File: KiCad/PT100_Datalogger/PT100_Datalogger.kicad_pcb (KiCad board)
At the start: 4 copper layers, 90 x 122 mm, 190 parts, among them J1 PWR, J10 Conn_01x03, J11 Conn_01x03, J12 Conn_01x03, J13 HLK-LD2410C, J14 691406710003B, J2 USB_C_Receptacle, J3 Screw_Terminal_01x02, J4 CT, J5 SJ1-3523N, J6 JTAG, J7 CT_SW, J8 Conn_01x03, J9 Conn_01x03, K1 J115F11CH5VDCS61.5U, Q10 BSS806NEH6327XTSA1, Q11 SSM3J36FS,LF, Q12 SSM3J36FS,LF, Q13 SSM3J36FS,LF, Q14 BSS806NEH6327XTSA1, Q15 SSM3J36FS,LF, Q16 MMBT3904, Q17 MMBT3904, Q3 BSS806NEH6327XTSA1, Q4 BSS806NEH6327XTSA1, Q5 BSS806NEH6327XTSA1, Q6 BSS806NEH6327XTSA1, Q7 BSS806NEH6327XTSA1, Q8 BSS806NEH6327XTSA1, Q9 BSS806NEH6327XTSA1, SW3 SW_Push_Shielded, SW4 SW_Push_Shielded, SW5 SW_Push_Shielded, SW6 SW_Push_Shielded, SW7 SW_Push_Shielded, U1 ESP32-S3-WROOM-1-N8R2, U10 SHT4x, U11 PCF85263AT, U12 FM24CL16B-GTR, U13 MCP9601, U2 CP2102N-Axx-xQFN28, U3 NCS2250SQ2T2G, U4 LDL212PV33R, U5 TMP1075DSG, U6 INND-TS56RAB, U7 INND-TS56RAB, U8 INND-TS56RAB, U9 INND-TS56RAB, Y1 32.768K12.5PI/3215E

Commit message: Finished KiCad PCB REV A
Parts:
- removed D10, D6: ESD5Z12T1G, Diode_SMD:D_SOD-523
- removed D26, D30, D31, D32, D33, D36: ESD5Z3V3, Diode_SMD:D_SOD-523
- removed D27, D37, D38: B5819W, Diode_SMD:D_SOD-123
- removed K1: J115F11CH5VDCS61.5U, Personal:J115FX
- removed MK2: ICS-43434, Sensor_Audio:InvenSense_ICS-43434-6_3.5x2.65mm
- removed Q10, Q14, Q3, Q4, Q5, Q6, Q7, Q8, Q9: BSS806NEH6327XTSA1, Package_TO_SOT_SMD:SOT-23-3
- removed Q11, Q12, Q13, Q15: SSM3J36FS,LF, Package_TO_SOT_SMD:SOT-416
- removed Q16, Q17: MMBT3904, Package_TO_SOT_SMD:SOT-23_Handsoldering
- removed R30, R32, R34, R36, R38, R40, R47, R51: 1K, Resistor_SMD:R_0603_1608Metric_Pad0.98x0.95mm_HandSolder
- removed R31, R33, R35, R37, R39, R46, R50, R57: 100K, Resistor_SMD:R_0603_1608Metric_Pad0.98x0.95mm_HandSolder
- removed R43: 1M, Resistor_SMD:R_0603_1608Metric_Pad0.98x0.95mm_HandSolder
- removed R44, R45: 10k, Resistor_SMD:R_0603_1608Metric_Pad0.98x0.95mm_HandSolder
- removed R48: 4K7, Resistor_SMD:R_0603_1608Metric_Pad0.98x0.95mm_HandSolder
- removed R49: 220R, Resistor_SMD:R_0603_1608Metric_Pad0.98x0.95mm_HandSolder
- removed R58, R59, R60: 51R, Resistor_SMD:R_0603_1608Metric_Pad0.98x0.95mm_HandSolder
- removed R62, R63, R64, R65, R66, R67, R68, R69: 22R, Resistor_SMD:R_0603_1608Metric_Pad0.98x0.95mm_HandSolder
- removed RV1: PV36Y102C01B00, Personal:TRIM_PV36Y102C01B00
- removed U11: PCF85263AT, Package_SO:SOIC-8_3.9x4.9mm_P1.27mm
- removed U12: FM24CL16B-GTR, Package_SO:SOIC-8_3.9x4.9mm_P1.27mm
- removed Y1: 32.768K12.5PI/3215E, Crystal:Crystal_SMD_3215-2Pin_3.2x1.5mm
- added C25: 100nF, Capacitor_SMD:C_0603_1608Metric_Pad1.08x0.95mm_HandSolder, F.Cu at (94.4, 141.1)
- added C26: 100nF, Capacitor_SMD:C_0603_1608Metric_Pad1.08x0.95mm_HandSolder, F.Cu at (105.0, 141.1)
- added C27: 100nF, Capacitor_SMD:C_0603_1608Metric_Pad1.08x0.95mm_HandSolder, F.Cu at (109.7, 129.3)
- added C28: 100nF, Capacitor_SMD:C_0603_1608Metric_Pad1.08x0.95mm_HandSolder, F.Cu at (101.3, 77.0)
- added C29: 10uF, Capacitor_SMD:C_0805_2012Metric_Pad1.18x1.45mm_HandSolder, F.Cu at (99.3, 77.5)
- added D14: TSD05CDYFR, Diode_SMD:D_SOD-323_HandSoldering, F.Cu at (63.8, 70.8)
- added D15: ESD5Z3V3, Diode_SMD:D_SOD-523, F.Cu at (91.6, 130.4)
- added JP3: SolderJumper_3_Bridged12, Jumper:SolderJumper-3_P1.3mm_Bridged12_RoundedPad1.0x1.5mm, F.Cu at (99.0, 130.7)
- added JP5: SolderJumper_3_Bridged12, Jumper:SolderJumper-3_P1.3mm_Bridged12_RoundedPad1.0x1.5mm, F.Cu at (88.4, 141.5)
- added JP6: SolderJumper_3_Bridged12, Jumper:SolderJumper-3_P1.3mm_Bridged12_RoundedPad1.0x1.5mm, F.Cu at (99.0, 141.5)
- added JP7: SolderJumper_3_Bridged12, Jumper:SolderJumper-3_P1.3mm_Bridged12_Pad1.0x1.5mm, F.Cu at (95.1, 91.6)
- added JP8: SolderJumper_2_Open, Jumper:SolderJumper-2_P1.3mm_Open_TrianglePad1.0x1.5mm, F.Cu at (99.9, 91.5)
- added JP9: SolderJumper_2_Open, Jumper:SolderJumper-2_P1.3mm_Open_TrianglePad1.0x1.5mm, F.Cu at (96.0, 96.3)
- C12, C7: value 10uF -> 100nF; footprint Capacitor_SMD:C_0805_2012Metric_Pad1.18x1.45mm_HandSolder -> Capacitor_SMD:C_0603_1608Metric_Pad1.08x0.95mm_HandSolder
- C14: value 100nF -> 22uF; footprint Capacitor_SMD:C_0603_1608Metric_Pad1.08x0.95mm_HandSolder -> Capacitor_SMD:C_0805_2012Metric_Pad1.18x1.45mm_HandSolder
- C15: value 10uF -> 22uF
- C6: value 10uF -> DE1B3RA471KN4AP01F; footprint Capacitor_SMD:C_0805_2012Metric_Pad1.18x1.45mm_HandSolder -> Capacitor_THT:C_Disc_D7.5mm_W5.0mm_P10.00mm
- D11, D8: value TSD05CDYFR -> ESD5Z12T1G; footprint Diode_SMD:D_SOD-323_HandSoldering -> Diode_SMD:D_SOD-523
- D12: value TSD05CDYFR -> ESD5Z3V3; footprint Diode_SMD:D_SOD-323_HandSoldering -> Diode_SMD:D_SOD-523
- D2: value LED -> TSD05CDYFR; footprint LED_THT:LED_D5.0mm -> Diode_SMD:D_SOD-323_HandSoldering
- D21, D4: footprint LED_THT:LED_D5.0mm -> LED_SMD:LED_0603_1608Metric_Pad1.05x0.95mm_HandSolder
- D3: value SM4007PL -> TSD05CDYFR; footprint Diode_SMD:D_SOD-123F -> Diode_SMD:D_SOD-323_HandSoldering
- D5: value SM4007PL -> B5819W; footprint Diode_SMD:D_SOD-123F -> Diode_SMD:D_SOD-123
- D9: value B5819W -> ESD5Z12T1G; footprint Diode_SMD:D_SOD-123 -> Diode_SMD:D_SOD-523
- H1: footprint MountingHole:MountingHole_3.2mm_M3 -> MountingHole:MountingHole_3.2mm_M3_Pad
- J10: value Conn_01x03 -> DIG3
- J11: value Conn_01x03 -> DIG4
- J12: value Conn_01x03 -> DIG5
- J13: value HLK-LD2410C -> DIG6; footprint Connector_Molex:Molex_KK-254_AE-6410-05A_1x05_P2.54mm_Vertical -> Connector_Molex:Molex_KK-254_AE-6410-03A_1x03_P2.54mm_Vertical
- J14: value 691406710003B -> PWR; footprint Personal:691406710003B -> Connector_JST:JST_VH_B3P-VH_1x03_P3.96mm_Vertical
- J2: value USB_C_Receptacle -> Conn_01x04; footprint Personal:CONN_CU3216SASBLR004-NH_CVI -> Connector_Molex:Molex_KK-254_AE-6410-04A_1x04_P2.54mm_Vertical
- J3: value Screw_Terminal_01x02 -> TC
- J4: value CT -> MSD-4-A; footprint Connector_Molex:Molex_KK-254_AE-6410-02A_1x02_P2.54mm_Vertical -> Personal:CUI_MSD-4-A
- J5: value SJ1-3523N -> CU3216SASBLR004-NH; footprint Connector_Audio:Jack_3.5mm_CUI_SJ1-3523N_Horizontal -> Personal:CONN_CU3216SASBLR004-NH_CVI
- J6: value JTAG -> RTD; footprint Connector_PinHeader_1.27mm:PinHeader_2x05_P1.27mm_Vertical -> Connector_Molex:Molex_KK-254_AE-6410-05A_1x05_P2.54mm_Vertical
- J7: value CT_SW -> MAX7219; footprint Connector_Molex:Molex_KK-254_AE-6410-02A_1x02_P2.54mm_Vertical -> Connector_Molex:Molex_KK-254_AE-6410-05A_1x05_P2.54mm_Vertical
- J8: value Conn_01x03 -> DIG1
- J9: value Conn_01x03 -> DIG2
- JP1: value SolderJumper_3_Open -> SolderJumper_3_Bridged12; footprint Jumper:SolderJumper-3_P1.3mm_Open_Pad1.0x1.5mm -> Jumper:SolderJumper-3_P1.3mm_Bridged12_RoundedPad1.0x1.5mm
- JP2: value SolderJumper_2_Open -> SolderJumper_3_Bridged12; footprint Jumper:SolderJumper-2_P1.3mm_Open_Pad1.0x1.5mm -> Jumper:SolderJumper-3_P1.3mm_Bridged12_RoundedPad1.0x1.5mm
- JP4: value SolderJumper_2_Bridged -> SolderJumper_3_Bridged12; footprint Jumper:SolderJumper-2_P1.3mm_Bridged_Pad1.0x1.5mm -> Jumper:SolderJumper-3_P1.3mm_Bridged12_RoundedPad1.0x1.5mm
- R15, R26, R28: value 1K -> 100R
- R16, R25, R27, R29: value 100K -> 100R
- R17: value 5k1 -> 10K
- R18: value 5k1 -> 100R
- R2: value 1K -> 10K
- R21: value 100K -> RN73H1JTTD3920A05
- R22: value 1K -> 330R
- R23: value 100K -> 5k1
- R24: value 1K -> 5k1
- R3: value 22K1 -> 10K
- R4: value 47K5 -> 10K
- R7: value 50R -> 100R
- R8: value 100 -> 100R
- SW3, SW4, SW5, SW6, SW7: footprint Personal:SW_1825955-6_TEC -> Button_Switch_SMD:SW_SPST_B3U-1100P
- U10: value SHT4x -> SHT45
- U2: value CP2102N-Axx-xQFN28 -> SN74LVC245APW; footprint Package_DFN_QFN:QFN-28-1EP_5x5mm_P0.5mm_EP3.35x3.35mm -> Package_SO:TSSOP-20_4.4x6.5mm_P0.65mm
- U3: value NCS2250SQ2T2G -> MAX31865xAP; footprint Package_TO_SOT_SMD:SOT-353_SC-70-5_Handsoldering -> Package_SO:SSOP-20_5.3x7.2mm_P0.65mm
- U5: value TMP1075DSG -> TPD2E001; footprint Package_SON:WSON-8-1EP_2x2mm_P0.5mm_EP0.9x1.6mm_ThermalVias -> Package_TO_SOT_SMD:SOT-553
- U6: value INND-TS56RAB -> TPD2E001; footprint Display_7Segment:7SegmentLED_LTS6760_LTS6780 -> Package_TO_SOT_SMD:SOT-553
- U7: value INND-TS56RAB -> CY15B104QN-50SXI; footprint Display_7Segment:7SegmentLED_LTS6760_LTS6780 -> Package_SO:SOIC-8_5.3x5.3mm_P1.27mm
- U8: value INND-TS56RAB -> PCF2131; footprint Display_7Segment:7SegmentLED_LTS6760_LTS6780 -> Personal:16-HLSON
- U9: value INND-TS56RAB -> TPD6E05U06RVZ; footprint Display_7Segment:7SegmentLED_LTS6760_LTS6780 -> Package_SON:Texas_R-PUSON-N14
- moved J1 183.2 mm to (57.3, 83.8)
- moved J5 177.1 mm to (61.0, 70.1), turned to -90 degrees
- moved D7 172.5 mm to (63.8, 84.0), turned to -90 degrees
- moved C1 171.2 mm to (66.5, 51.0), turned to -90 degrees
- moved C2 171.1 mm to (64.7, 51.2), turned to -90 degrees
- moved C8 167.0 mm to (73.5, 75.0), turned to 90 degrees
- moved H3 164.9 mm to (56.5, 148.0)
- moved C21 164.9 mm to (70.9, 79.9), turned to 0 degrees
- moved C5 164.6 mm to (54.0, 64.7), turned to -90 degrees
- moved C4 162.4 mm to (54.0, 59.8), turned to -90 degrees
- moved D29 162.3 mm to (55.5, 64.7), turned to -90 degrees
- moved C3 160.9 mm to (62.0, 61.4)
- moved D28 160.1 mm to (55.5, 59.8), turned to -90 degrees
- moved D5 160.0 mm to (63.8, 79.3), turned to 90 degrees
- moved R1 155.2 mm to (62.0, 63.0)
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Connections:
- C10 pad 1: TEMP_DOWN -> STOP
- C11 pad 1: SOFT_ON_OFF -> UNITS
- C12 pad 1: Net-(D27-K) -> Net-(JP9-A)
- C12 pad 2: GND -> Net-(JP8-B)
- C13 pad 1: Net-(D16-A2) -> +3V3
- C14 pad 1: +3V3 -> Net-(U8-IFS)
- C15 pad 1: Net-(J4-Pin_1) -> Net-(U8-IFS)
- C15 pad 2: Net-(D27-A) -> GND
- C16 pad 1: CT -> +5V
- C18 pad 1: +3V3 -> DIGITAL_2
- C20 pad 1: +3V3 -> DIGITAL_3
- C21 pad 1: +3V3 -> Net-(U8-IFS)
- C24 pad 1: +3V3 -> DIGITAL_4
- C6 pad 1: +3V3 -> Earth_Clean
- C7 pad 1: Net-(U2-VBUS) -> DIGITAL_1
- C9 pad 1: TEMP_UP -> START
- D1 pad 1: GND -> VSense
- D1 pad 2: VSense -> GND
- D11 pad 1: GND -> Net-(D11-K)
- D11 pad 2: USB_D+ -> GND
- D12 pad 1: GND -> SD_SW
- D12 pad 2: USB_D- -> GND
- D13 pad 1: GND -> Net-(D13-K)
- D13 pad 2: Net-(D13-A2) -> GND
- D16 pad 1: GND -> Net-(D16-K)
- D16 pad 2: Net-(D16-A2) -> GND
- D17 pad 1: GND -> Net-(D17-K)
- D17 pad 2: Net-(D17-A2) -> GND
- D18 pad 1: GND -> Net-(D18-K)
- D18 pad 2: Net-(D18-A2) -> GND
- D19 pad 1: GND -> Net-(D19-K)
- D19 pad 2: Net-(D19-A2) -> GND
- D2 pad 1: Net-(D2-K) -> GND
- D2 pad 2: Net-(D2-A) -> USB_D-
- D22 pad 1: GND -> Net-(D22-K)
- D22 pad 2: ONEWIRE -> GND
- D23 pad 1: GND -> Net-(D23-K)
- D23 pad 2: MTMS -> GND
- D24 pad 1: GND -> Net-(D24-K)
- D24 pad 2: MTCK -> GND
- D25 pad 1: GND -> Net-(D25-K)
- D25 pad 2: MTDO -> GND
- D28 pad 1: GND -> GPIO0
- D28 pad 2: GPIO0 -> GND
- D29 pad 1: GND -> CHIP_PU
- D29 pad 2: CHIP_PU -> GND
- D3 pad 1: +5V -> GND
- D3 pad 2: Net-(D2-K) -> VBUS
- D34 pad 1: GND -> U0RXD
- D34 pad 2: U1TX -> GND
- D35 pad 1: GND -> U0TXD
- D35 pad 2: U1RX -> GND
- D5 pad 1: +3V3 -> +5V
- D5 pad 2: Net-(D27-K) -> VBUS
- D8 pad 1: GND -> Net-(D8-K)
- D8 pad 2: VBUS -> GND
- D9 pad 1: +5V -> Net-(D9-K)
- D9 pad 2: VBUS -> GND
- H3 pad 1: GND -> unconnected-(H3-Pad1)
- J10 pad 1: +3V3 -> Net-(J10-Pin_1)
- J10 pad 2: ONEWIRE -> Net-(D22-K)
- J11 pad 1: +3V3 -> Net-(J11-Pin_1)
- J11 pad 2: ONEWIRE -> Net-(D23-K)
- J12 pad 1: +3V3 -> Net-(J12-Pin_1)
- J12 pad 2: ONEWIRE -> Net-(D24-K)
- J13 pad 1: U1RX -> Net-(J13-Pin_1)
- J13 pad 2: U1TX -> Net-(D25-K)
- J13 pad 3: MM_OUT -> GND
- J14 pad 3: AC_OUT -> Earth_Clean
- J3 pad 1: GND -> Net-(D13-K)
- J3 pad 3: Net-(D13-A2) -> GND
- J4 pad 1: Net-(J4-Pin_1) -> SD_D2
- J4 pad 2: GND -> SD_D3
- J6 pad 1: +3V3 -> GND
- J6 pad 2: MTMS -> RTD_FN
- J6 pad 3: GND -> RTD_INN
- J6 pad 4: MTCK -> RTD_INP
- J6 pad 5: GND -> RTD_FP
- J7 pad 1: CT -> +5V
- J8 pad 1: +3V3 -> Net-(J8-Pin_1)
- J8 pad 2: ONEWIRE -> Net-(D16-K)
- J9 pad 1: +3V3 -> Net-(J9-Pin_1)
- J9 pad 2: ONEWIRE -> Net-(D15-K)
- JP1 pad 1: Net-(JP1-A) -> +3V3
- JP1 pad 2: Net-(D16-A2) -> Net-(J8-Pin_1)
- JP1 pad 3: CT -> +5V
- JP2 pad 1: Net-(JP2-A) -> +3V3
- JP2 pad 2: CT -> Net-(J9-Pin_1)
- JP4 pad 1: Net-(JP4-A) -> +3V3
- JP4 pad 2: CHIP_PU -> Net-(J11-Pin_1)
- R10 pad 1: Net-(D17-A2) -> Net-(D17-K)
- R11 pad 1: Net-(D18-A2) -> Net-(D18-K)
- R12 pad 1: Net-(D18-A2) -> Net-(D18-K)
- R12 pad 2: TEMP_DOWN -> STOP
- R13 pad 1: Net-(D19-A2) -> Net-(D19-K)
- R14 pad 1: Net-(D19-A2) -> Net-(D19-K)
- R14 pad 2: SOFT_ON_OFF -> UNITS
- R15 pad 1: SEG_A -> Net-(JP8-B)
- R15 pad 2: Net-(Q3-G) -> RTD_INN
- R16 pad 1: GND -> Net-(JP8-A)
- R16 pad 2: SEG_A -> RTD_FN
- R17 pad 1: Net-(J2-CC1) -> +3V3
- R17 pad 2: GND -> SD_D1
- R18 pad 1: Net-(J2-CC2) -> Net-(D15-K)
- R18 pad 2: GND -> DIGITAL_2
- R2 pad 2: Net-(U2-~{RST}) -> SD_D2
- R21 pad 1: GND -> Net-(U3-BIAS)
- R21 pad 2: SEG_B -> Net-(U3-ISENSOR)
- R22 pad 1: SEG_B -> +3V3
- R22 pad 2: Net-(Q4-G) -> Net-(U8-IFS)
- R23 pad 1: GND -> Net-(J5-CC1)
- R23 pad 2: SEG_C -> GND
- R24 pad 1: SEG_C -> Net-(J5-CC2)
- R24 pad 2: Net-(Q5-G) -> GND
- R25 pad 1: GND -> Net-(D16-K)
- R25 pad 2: SEG_D -> DIGITAL_1
- R26 pad 1: SEG_D -> Net-(D22-K)
- R26 pad 2: Net-(Q6-G) -> DIGITAL_3
- R27 pad 1: GND -> Net-(D23-K)
- R27 pad 2: SEG_E -> DIGITAL_4
- R28 pad 1: SEG_E -> Net-(D24-K)
- R28 pad 2: Net-(Q7-G) -> DIGITAL_5
- R29 pad 1: GND -> Net-(D25-K)
- R29 pad 2: SEG_F -> DIGITAL_6
- R3 pad 1: VBUS -> +3V3
- R3 pad 2: Net-(U2-VBUS) -> SD_D3
- R4 pad 1: Net-(U2-VBUS) -> +3V3
- R4 pad 2: GND -> SD_CMD
- R5 pad 1: DTR -> +3V3
- R5 pad 2: Net-(Q16-B) -> SD_CLK
- R52 pad 1: Net-(D13-A2) -> Net-(D13-K)
- R56 pad 1: Net-(D13-A2) -> Net-(D13-K)
- R6 pad 1: RTS -> +3V3
- R6 pad 2: Net-(Q17-B) -> SD_D0
- R7 pad 1: Net-(J4-Pin_1) -> Net-(JP7-B)
- R7 pad 2: GND -> RTD_FP
- R8 pad 1: Net-(D27-K) -> Net-(JP9-A)
- R8 pad 2: Net-(D16-A2) -> RTD_INP
- R9 pad 1: Net-(D17-A2) -> Net-(D17-K)
- R9 pad 2: TEMP_UP -> START
- SW3 pad 2: Net-(D17-A2) -> Net-(D17-K)
- SW4 pad 2: Net-(D18-A2) -> Net-(D18-K)
- SW5 pad 2: Net-(D19-A2) -> Net-(D19-K)
- U1 pad 10: U1TX -> DIGITAL_4
- U1 pad 11: U1RX -> LEVEL_OE
- U1 pad 13: SEG_DP -> USB_D-
- U1 pad 14: ALERT -> USB_D+
- U1 pad 18: SEG_A -> MAX_CS
- U1 pad 19: SEG_B -> MOSI
- U1 pad 20: SEG_C -> SCK
- U1 pad 21: SEG_D -> MISO
- U1 pad 22: SEG_E -> DIGITAL_2
- U1 pad 23: DIG_1 -> DIGITAL_5
- U1 pad 24: DIG_2 -> D_CS
- U1 pad 25: DIG_3 -> SD_SW
- U1 pad 28: Net-(U1-IO35) -> SD_D1
- U1 pad 29: I2S_D -> SD_D0
- U1 pad 30: Net-(U1-IO37) -> SD_CLK
- U1 pad 31: RELAY_PWR -> SD_CMD
- U1 pad 32: MTCK -> SD_D3
- U1 pad 33: MTDO -> SD_D2
- U1 pad 34: MTDI -> ~{MAX_RDY}
- U1 pad 35: MTMS -> DIGITAL_6
- U1 pad 38: DIG_4 -> RTC_INT
- U1 pad 39: ONEWIRE -> 1HZ
- U1 pad 4: SOFT_ON_OFF -> DIGITAL_1
- U1 pad 5: TEMP_DOWN -> START
- U1 pad 6: TEMP_UP -> STOP
- U1 pad 7: CT -> UNITS
- U1 pad 8: SEG_F -> FRAM_CS
- U1 pad 9: SEG_G -> DIGITAL_3
- U2 pad 1: unconnected-(U2-~{DCD}-Pad1) -> +5V
- U2 pad 10: unconnected-(U2-NC-Pad10) -> GND
- U2 pad 16: unconnected-(U2-~{WAKEUP}/GPIO.3-Pad16) -> Net-(D8-K)
- U2 pad 17: unconnected-(U2-RS485/GPIO.2-Pad17) -> Net-(D9-K)
- U2 pad 18: unconnected-(U2-~{RXT}/GPIO.1-Pad18) -> Net-(D11-K)
- U2 pad 19: unconnected-(U2-~{TXT}/GPIO.0-Pad19) -> LEVEL_OE
- U2 pad 2: unconnected-(U2-~{RI}/CLK-Pad2) -> MOSI
- U2 pad 20: unconnected-(U2-GPIO.6-Pad20) -> +5V
- U2 pad 3: GND -> D_CS
- U2 pad 4: USB_D+ -> SCK
- U2 pad 5: USB_D- -> GND
- U2 pad 6: +3V3 -> GND
- U2 pad 7: +3V3 -> GND
- U2 pad 8: Net-(U2-VBUS) -> GND
- U2 pad 9: Net-(U2-~{RST}) -> GND
- U3 pad 1: Net-(JP2-A) -> ~{MAX_RDY}
- U3 pad 2: GND -> +3V3
- U3 pad 3: Net-(JP1-A) -> +3V3
- U3 pad 4: Net-(U3--) -> Net-(U3-BIAS)
- U3 pad 5: +3V3 -> Net-(U3-BIAS)
- U5 pad 1: SDA -> +3V3
- U5 pad 2: SCL -> unconnected-(U5-NC-Pad2)
- U5 pad 3: RELAY_ALERT -> RTD_INP
- U5 pad 5: GND -> RTD_FP
- U6 pad 1: SEG_E_LED -> +3V3
- U6 pad 2: SEG_D_LED -> unconnected-(U6-NC-Pad2)
- U6 pad 3: DIG_1_LED -> RTD_FN
- U6 pad 4: SEG_C_LED -> GND
- U6 pad 5: SEG_DP_LED -> RTD_INN
- U7 pad 1: SEG_E_LED -> FRAM_CS
- U7 pad 2: SEG_D_LED -> MISO
- U7 pad 3: DIG_2_LED -> +3V3
- U7 pad 4: SEG_C_LED -> GND
- U7 pad 5: SEG_DP_LED -> MOSI
- U7 pad 6: SEG_B_LED -> SCK
- U7 pad 7: SEG_A_LED -> unconnected-(U7-~{HOLD}-Pad7)
- U7 pad 8: DIG_2_LED -> +3V3
- U8 pad 1: SEG_E_LED -> Net-(U8-IFS)
- U8 pad 10: SEG_G_LED -> unconnected-(U8-~{TS3}-Pad10)
- U8 pad 2: SEG_D_LED -> SCL
- U8 pad 3: DIG_3_LED -> GND
- U8 pad 4: SEG_C_LED -> GND
- U8 pad 5: SEG_DP_LED -> SDA
- U8 pad 6: SEG_B_LED -> 1HZ
- U8 pad 7: SEG_A_LED -> GND
- U8 pad 8: DIG_3_LED -> unconnected-(U8-~{TS1}-Pad8)
- U8 pad 9: SEG_F_LED -> unconnected-(U8-~{TS2}-Pad9)
- U9 pad 1: SEG_E_LED -> SD_D2
- U9 pad 10: SEG_G_LED -> GND
- U9 pad 2: SEG_D_LED -> SD_D3
- U9 pad 3: DIG_4_LED -> SD_CMD
- U9 pad 4: SEG_C_LED -> SD_CLK
- U9 pad 5: SEG_DP_LED -> GND
- U9 pad 6: SEG_B_LED -> SD_D0
- U9 pad 7: SEG_A_LED -> SD_D1
- U9 pad 8: DIG_4_LED -> SD_D1
- U9 pad 9: SEG_F_LED -> SD_D0
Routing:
- net ONEWIRE: track 163.7 -> 0.00 mm, vias 2 -> 0
- net SEG_E_LED: track 116.2 -> 0.00 mm, vias 2 -> 0
- net DIGITAL_4: track 0.00 -> 102.3 mm, vias 0 -> 2
- net DIGITAL_6: track 0.00 -> 99.2 mm, vias 0 -> 2
- net DIGITAL_1: track 0.00 -> 98.3 mm, vias 0 -> 2
- net SEG_C_LED: track 95.7 -> 0.00 mm, vias 1 -> 0
- net SEG_D_LED: track 94.7 -> 0.00 mm, vias 1 -> 0
- net SEG_DP_LED: track 94.6 -> 0.00 mm, vias 1 -> 0
- net DIGITAL_3: track 0.00 -> 93.8 mm, vias 0 -> 2
- net RELAY_ALERT: track 87.0 -> 0.00 mm, vias 2 -> 0
- net START: track 0.00 -> 87.0 mm, vias 0 -> 2
- net UNITS: track 0.00 -> 86.7 mm, vias 0 -> 2
- net STOP: track 0.00 -> 85.0 mm, vias 0 -> 2
- net DIGITAL_5: track 0.00 -> 81.8 mm, vias 0 -> 2
- net SEG_E: track 80.9 -> 0.00 mm, vias 3 -> 0
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- removed copper zone on B.Cu, net AC_OUT
- removed copper zone on F.Cu, net AC_OUT
- removed copper zone on In1.Cu, net AC_OUT
- removed copper zone on In2.Cu, net AC_OUT
- removed copper zone on F.Cu, net GND
- removed copper zone on In2.Cu, net GND
- removed copper zone on B.Cu, net L1
- removed copper zone on F.Cu, net L1
- removed copper zone on In1.Cu, net L1
- removed copper zone on In2.Cu, net L1
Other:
- board size 90 x 122 mm -> 62 x 105 mm
- board text added: "1) NEUTRAL 2) LINE 3) EARTH"
- board text added: "2-Wire"
- board text added: "2/3"
- board text added: "2/4"
- board text added: "250v/2A Slow Blow 5x20mm"
- board text added: "3-Wire"
- board text added: "3v3/5 SW GND"
- board text added: "5v GND"
- board text added: "5v GND MOSI CS SCK"
- board text added: "BOOT0"
- board text added: "DIG1"
- board text added: "DIG2"
- board text added: "DIG3"
- board text added: "DIG4"
- board text added: "DIG5"
- board text added: "DIG6"
- board text added: "GND F- IN- IN+ F+"
- board text added: "MAX7219"
- board text added: "PT100"
- board text added: "PT100 Datalogger+ PlantInsight Rev A Robert Susmilch"
- board text added: "SHT45"
- board text added: "START"
- board text added: "STOP"
- board text added: "TC- TC+ GND"
- board text added: "TX RX GND 5v"
- board text added: "Thermocouple"
- board text added: "UART"
- board text added: "UNITS"
- board text removed: "3v3 GND GND GND GND"
- board text removed: "5v GND MM_OUT U1TX U1RX"
- board text removed: "DOWN"
- board text removed: "GND 5V"
- board text removed: "GND CT_ANA"
- board text removed: "GND CT_SW"
- board text removed: "GND ONEWIRE 3v3"
- board text removed: "GPIO0"
- board text removed: "JLCJLCJLCJLC"
- board text removed: "JTAG"
- board text removed: "MTMS MTCK MTDO MTDI x"
- board text removed: "OUT LINE NEUT"
- board text removed: "PWR"
- board text removed: "Pot"
- board text removed: "RELAY"
- board text removed: "Smart Thermostat Node v1.0, 05/2025 Robert Susmilch"
- board text removed: "UP"

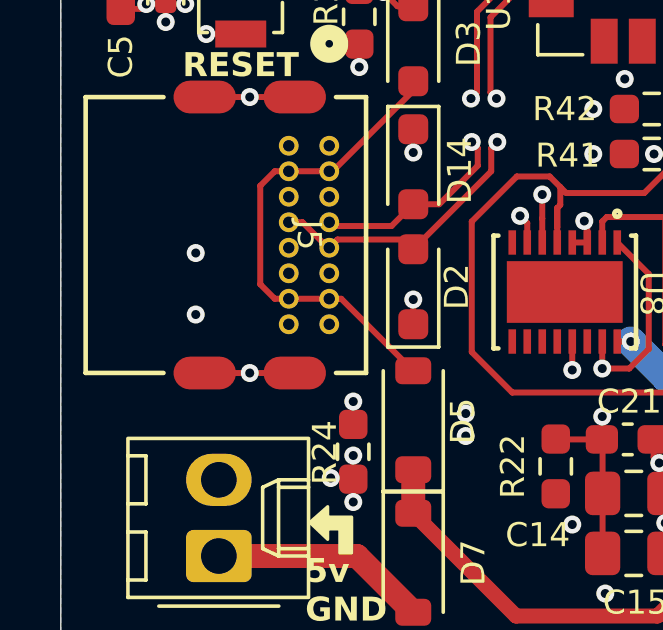
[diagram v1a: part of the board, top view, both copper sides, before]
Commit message: Removed extra iterations of plotter files. Refactored directories so updated gitignore.
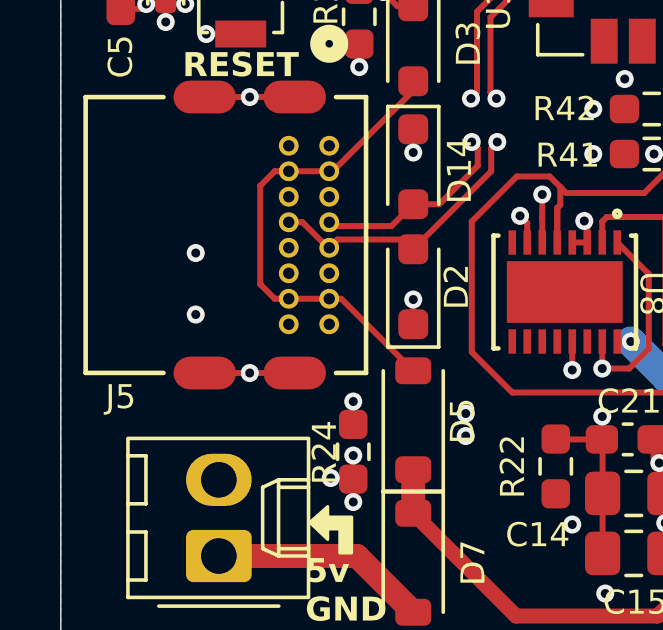
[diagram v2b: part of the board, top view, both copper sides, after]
